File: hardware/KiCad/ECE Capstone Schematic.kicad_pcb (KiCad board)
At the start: 2 copper layers, 46 parts, among them J2 Conn_01x08, J3 Conn_01x02, SW1 RESET, SW2 SW_BOOT, SW3 USER_BUTTON, U1 4525DO-DS5AI001DP, U2 ESP32-S3-WROOM-1U-N8R8, U3 TPS22919DCKT, U4 BMI088, U5 MCP73831-2-OT, U6 LM27313XMF

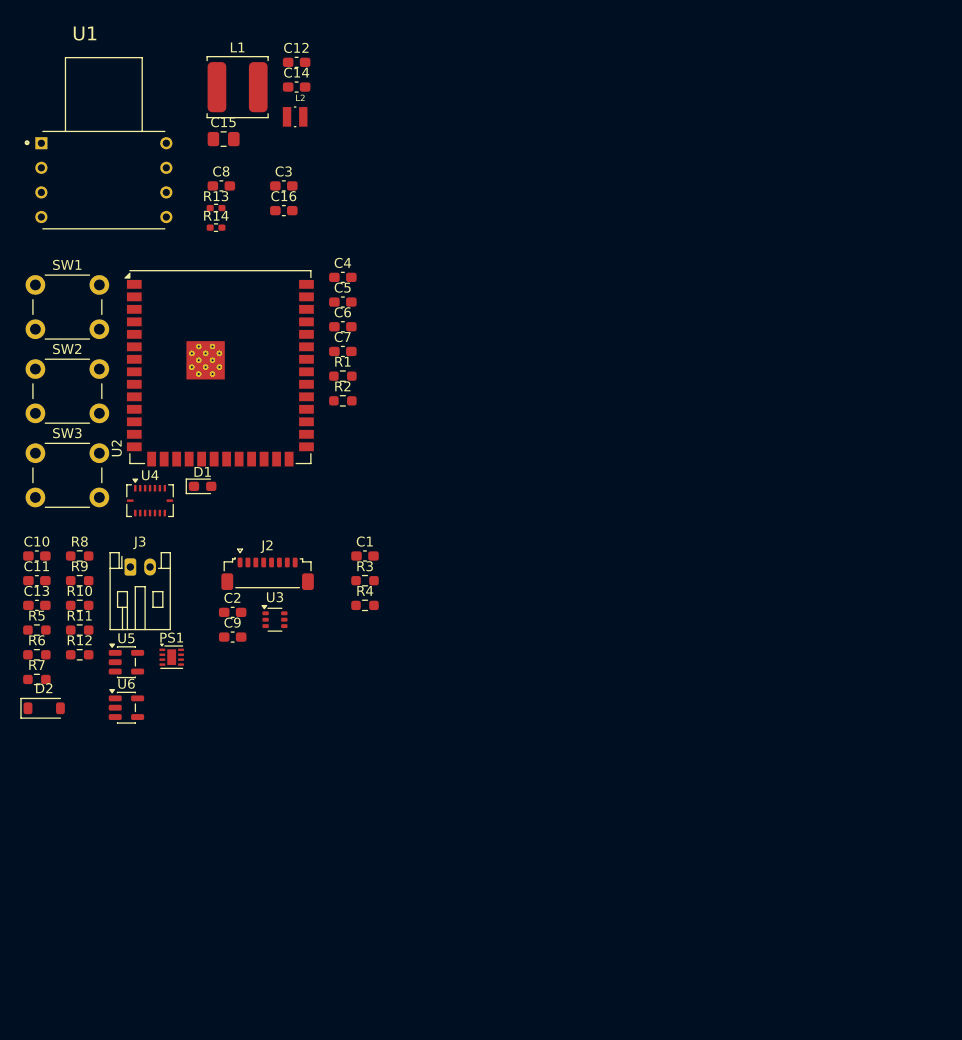
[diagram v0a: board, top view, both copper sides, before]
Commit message: Update PCB power schematic and custom footprints
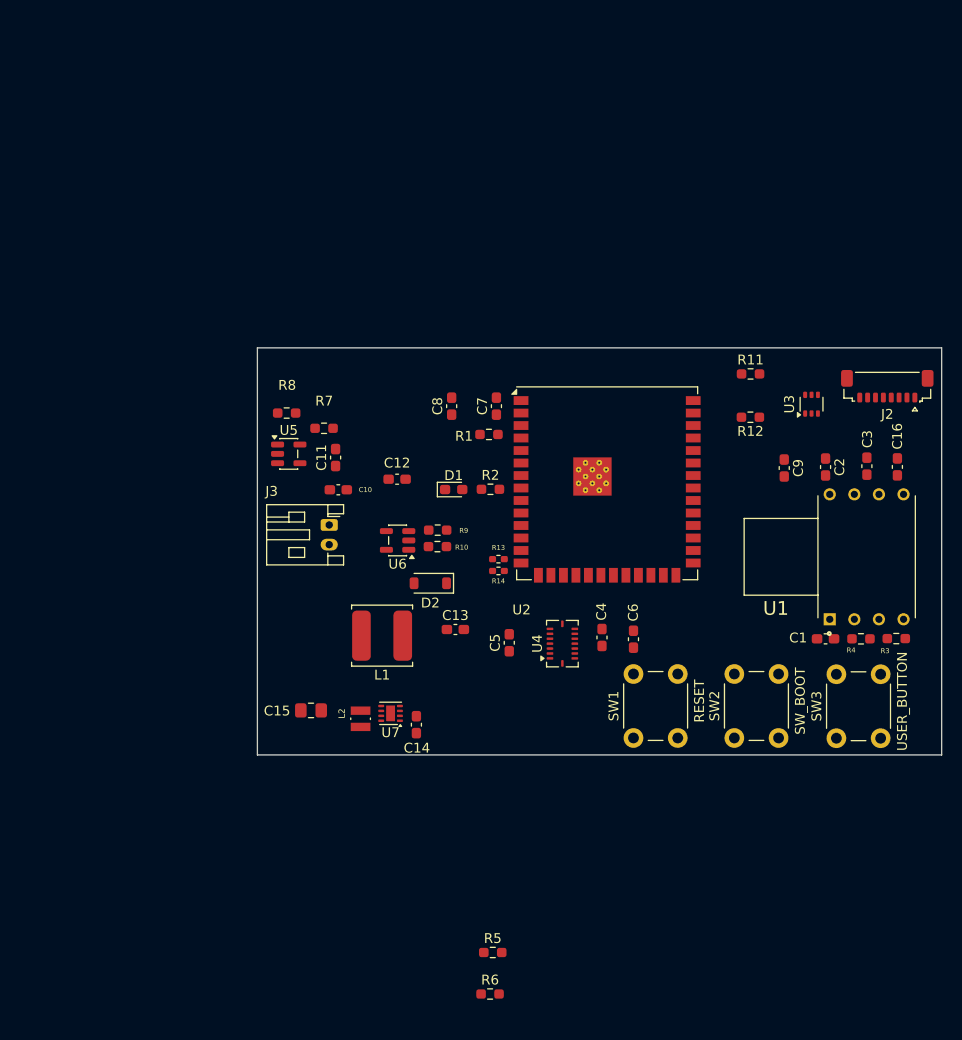
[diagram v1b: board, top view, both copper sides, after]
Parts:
- moved U1 86.5 mm to (212.8, 89.8), turned to 90 degrees
- moved SW3 86.4 mm to (209.8, 108.2), turned to 90 degrees
- moved SW2 80.3 mm to (199.4, 108.2), turned to 90 degrees
- moved SW1 76.3 mm to (189.1, 108.2), turned to 90 degrees
- moved R11 73.0 mm to (201.0, 71.2)
- moved R12 72.3 mm to (201.0, 75.6), turned to 180 degrees
- moved C16 67.6 mm to (215.9, 80.7), turned to -90 degrees
- moved C14 65.9 mm to (167.1, 106.9), turned to 90 degrees
- moved J2 65.8 mm to (214.9, 72.5), turned to 180 degrees
- moved C3 65.8 mm to (212.8, 80.6), turned to -90 degrees
- moved C2 62.0 mm to (208.7, 80.7), turned to -90 degrees
- moved L2 61.5 mm to (161.4, 106.3), turned to 90 degrees
- moved U3 58.8 mm to (207.2, 74.3), turned to 90 degrees
- moved C15 58.7 mm to (156.3, 105.4)
- moved C9 58.6 mm to (204.4, 80.8), turned to -90 degrees
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- renumbered PS1 to U7
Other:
- board outline added: 69.5 x 41.4 mm

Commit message: Update KiCad schematics and PCB footprints
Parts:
- added C17: 1uF, Capacitor_SMD:C_0603_1608Metric_Pad1.08x0.95mm_HandSolder, F.Cu at (192.0, 127.8)
- added C18: 10uF, Capacitor_SMD:C_0805_2012Metric_Pad1.18x1.45mm_HandSolder, F.Cu at (192.3, 125.0)
- added J7: UART_PROG, Connector_PinHeader_2.54mm:PinHeader_1x04_P2.54mm_Vertical, F.Cu at (199.0, 125.8)
- added R15: 10 K, Resistor_SMD:R_0603_1608Metric_Pad0.98x0.95mm_HandSolder, F.Cu at (203.4, 124.7)
- added R16: 10 K, Resistor_SMD:R_0603_1608Metric_Pad0.98x0.95mm_HandSolder, F.Cu at (203.4, 127.2)
- added TP1: 3V3_TEST, TestPoint:TestPoint_Pad_D1.5mm, F.Cu at (188.1, 125.3)
- added TP2: 5V_TEST, TestPoint:TestPoint_Pad_D1.5mm, F.Cu at (188.1, 128.8)
- added TP3: VBAT_TEST, TestPoint:TestPoint_Pad_D1.5mm, F.Cu at (188.1, 132.4)
- added TP4: GND_TEST, TestPoint:TestPoint_Pad_D1.5mm, F.Cu at (188.1, 135.9)
- C1, C2: footprint Capacitor_SMD:C_0603_1608Metric_Pad1.08x0.95mm_HandSolder -> Capacitor_SMD:C_0201_0603Metric_Pad0.64x0.40mm_HandSolder
- C12: value 2.2uF -> 1uF
- C15: value 22uF -> 10uF
- C4, C5: value 100 nF -> 100nF; footprint Capacitor_SMD:C_0603_1608Metric_Pad1.08x0.95mm_HandSolder -> Capacitor_SMD:C_0201_0603Metric_Pad0.64x0.40mm_HandSolder
- C6: value 1 uF -> 1uF
- C7: value 0.1uF -> 100nF; footprint Capacitor_SMD:C_0603_1608Metric_Pad1.08x0.95mm_HandSolder -> Capacitor_SMD:C_0201_0603Metric_Pad0.64x0.40mm_HandSolder
- R2: value 1K -> 470
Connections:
- J2 pad 1: LIDAR_RX -> LIDAR_TX
- J2 pad 2: LIDAR_TX -> LIDAR_RX
- U2 pad 36: unconnected-(U2-RXD0-Pad36) -> /MCU+IMU/RXDO
- U2 pad 37: unconnected-(U2-TXD0-Pad37) -> /MCU+IMU/TXDO
